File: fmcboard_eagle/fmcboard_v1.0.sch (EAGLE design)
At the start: 7 parts, among them J1 8pin, J12 4p-2.54, J2 ASP-134604-01

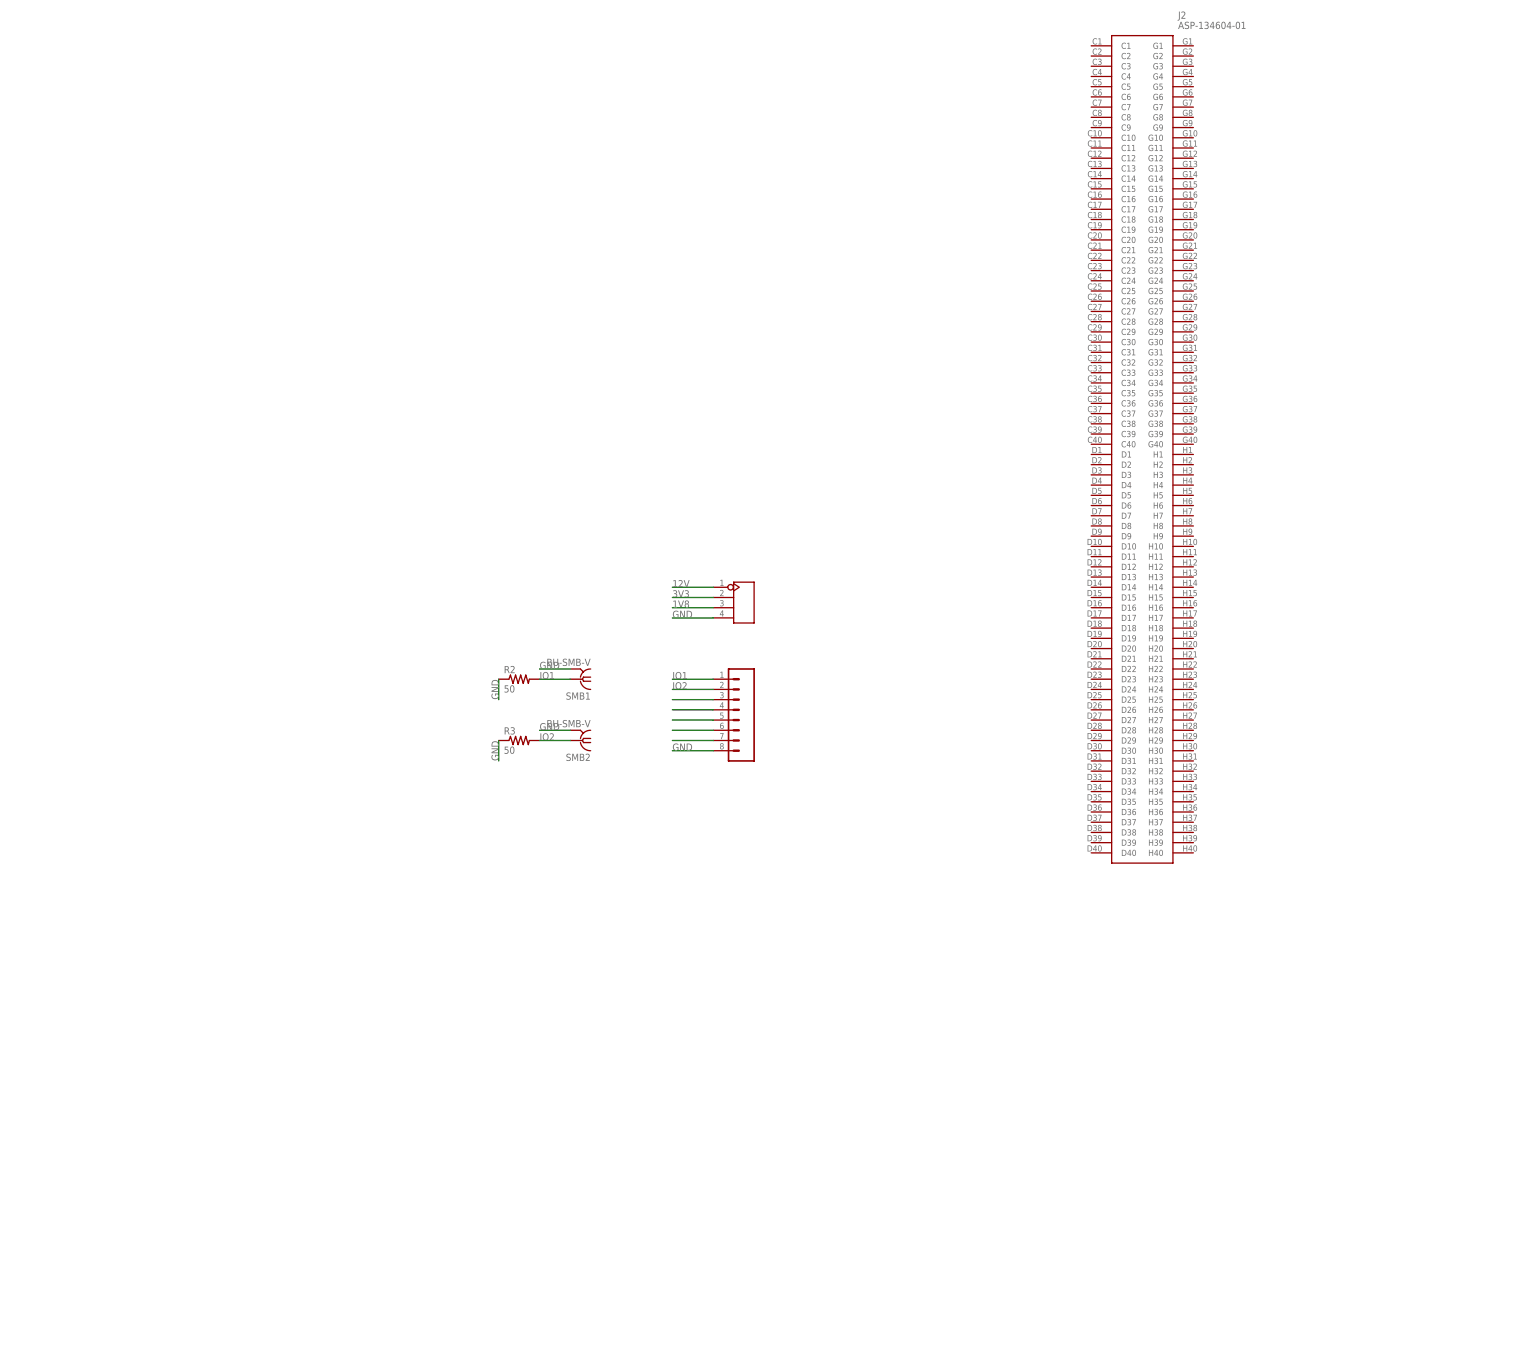
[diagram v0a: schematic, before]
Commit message: added two op amps to condition input and added GPIO breakout
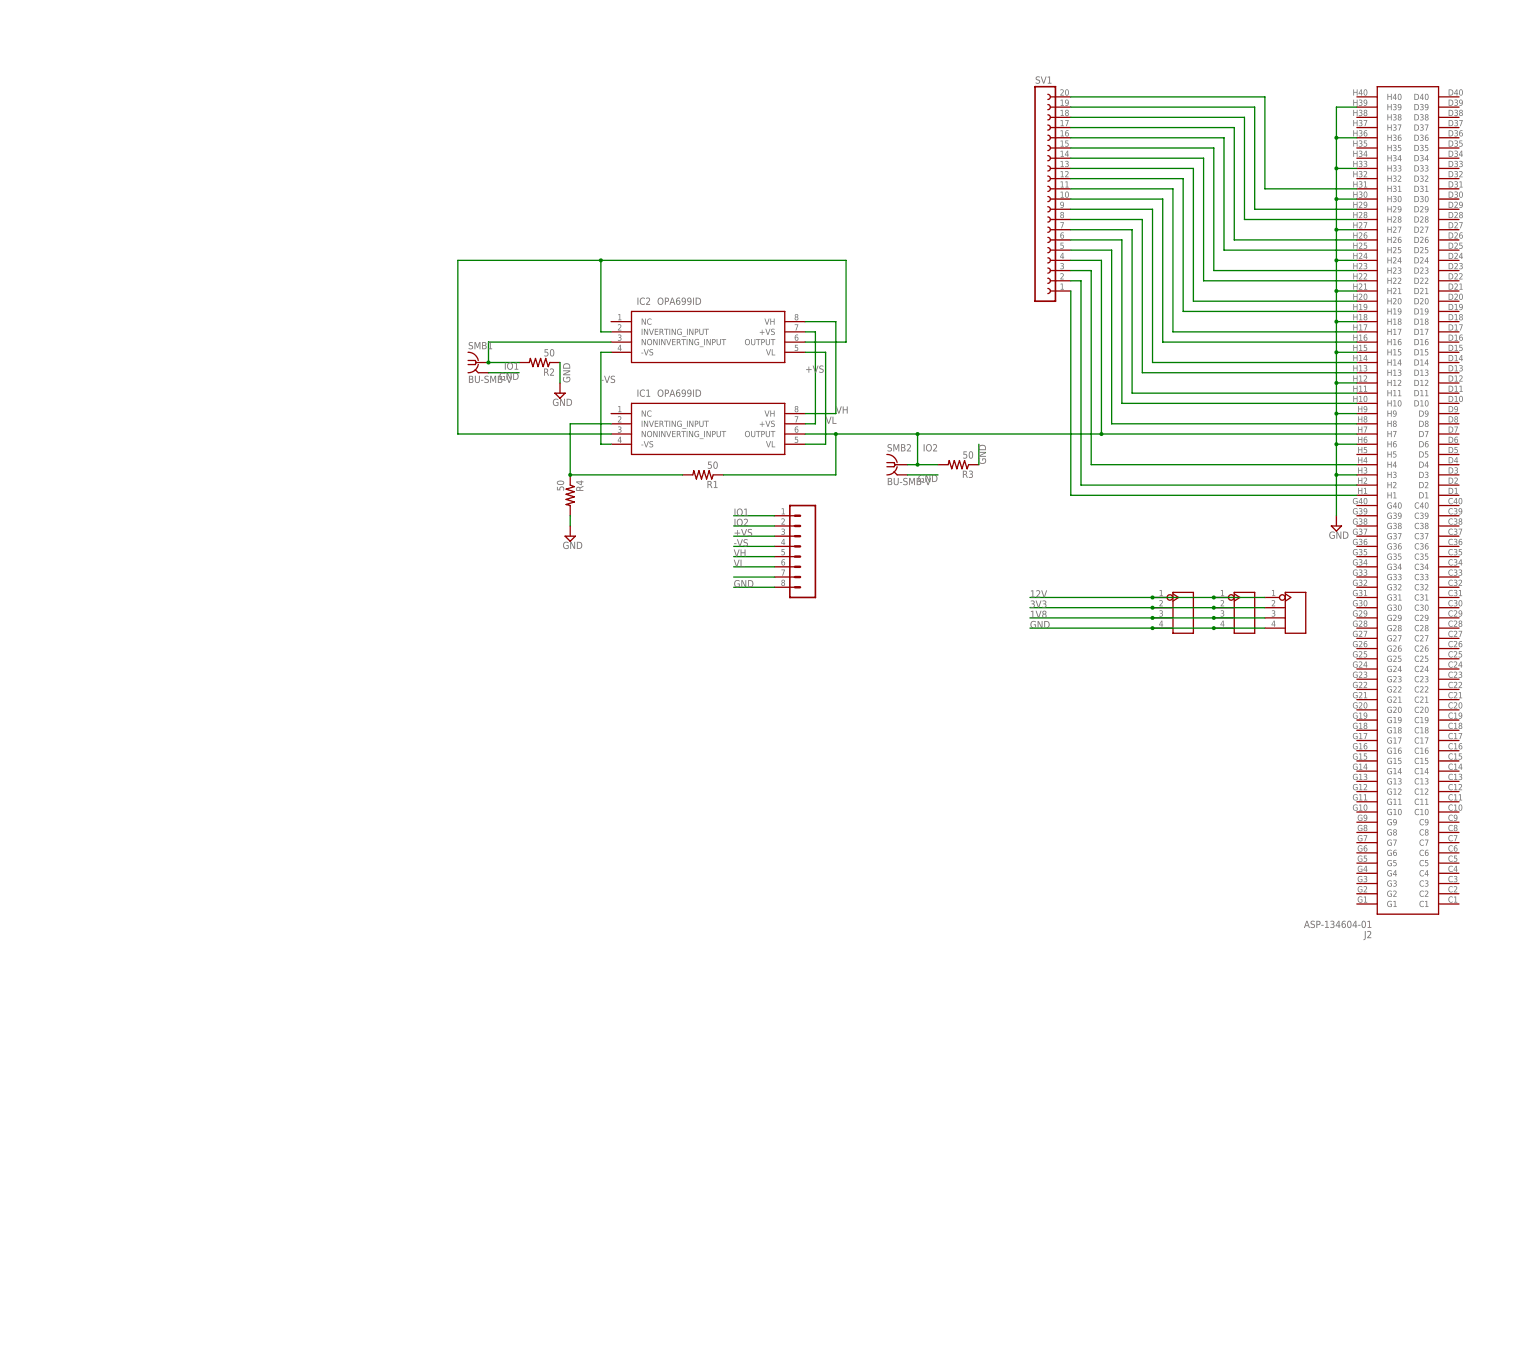
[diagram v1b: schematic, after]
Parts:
- added IC1, IC2: OPA699ID, OPA699ID:OPA699ID
- added J3, J4: 4p-2.54, Seeed-Connector:DIP-BLACK-FEMALE-HEADER-VERT(4P-2.54)
- added R1, R4: 50, SparkFun-Resistors:RESISTORAXIAL-0.3
- added SV1: (no value), con-lsta:FE20-1
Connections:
- removed net N$2: J1.3
- removed net N$4: J1.5
- removed net N$5: J1.4
- removed net N$6: J1.6
- new net +VS: IC1.+VS, IC2.+VS, J1.3
- new net -VS: IC1.-VS, IC2.-VS, J1.4
- new net N$1: IC1.NONINVERTING_INPUT, IC2.INVERTING_INPUT, IC2.OUTPUT
- new net N$10: J2.H8, SV1.5
- new net N$11: J2.H4, SV1.3
- new net N$12: J2.H10, SV1.6
- new net N$13: J2.H11, SV1.7
- new net N$14: J2.H13, SV1.8
- new net N$15: J2.H14, SV1.9
- new net N$16: J2.H16, SV1.10
- new net N$17: J2.H17, SV1.11
- new net N$18: J2.H19, SV1.12
- new net N$19: J2.H20, SV1.13
- new net N$20: J2.H22, SV1.14
- new net N$21: J2.H23, SV1.15
- new net N$22: J2.H25, SV1.16
- new net N$23: J2.H26, SV1.17
- new net N$24: J2.H28, SV1.18
- new net N$25: J2.H29, SV1.19
- new net N$26: J2.H31, SV1.20
- new net N$3: IC1.INVERTING_INPUT, R1.2, R4.1
- new net N$8: J2.H1, SV1.1
- new net N$9: J2.H2, SV1.2
- new net VH: IC1.VH, IC2.VH, J1.5
- new net VL: IC1.VL, IC2.VL, J1.6
- net 12V: now also J3.P$1, J4.P$1
- net 1V8: now also J3.P$3, J4.P$3
- net 3V3: now also J3.P$2, J4.P$2
- net GND: now also J2.H12, J2.H15, J2.H18, J2.H21, J2.H24, J2.H27, J2.H3, J2.H30, J2.H33, J2.H36, J2.H39, J2.H6, J2.H9, J3.P$4, J4.P$4, R4.2
- net IO1: now also IC2.NONINVERTING_INPUT
- net IO2: now also IC1.OUTPUT, J2.H7, R1.1, SV1.4
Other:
- moved on the sheet: J2, R2, R3, SMB1, SMB2

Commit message: board v1 work with Andre
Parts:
- added C1, C2, C4, C6: 10uF, SparkFun-Capacitors:CAPPTH1
- added C10, C11, C12, C13, C14, C3, C5, C7, C8, C9: 0.1uF, SparkFun-Passives:CAP0805
- added IC3, IC4: ICL7660CPA, maxim:ICL7660CPA
- added J5: 8pin, SparkFun-Connectors:CONN_08"
- added PCB1: ARDUINO_NANO, E14_Arduino_revC:ARDUINO_NANO
- added R5: 10k, SparkFun-Resistors:RESISTORAXIAL-0.3
- added R6: 50, SparkFun-Resistors:RESISTORAXIAL-0.3
- added R7, R8: 100k, resistor:R-TRIMM3296W
- added SMB3: BU-SMB-V, con-coax:BU-SMB-V
- added SV2: 20, con-lsta:FE20-1
- added U1: TXS0108EPWR-TSSOP20, Seeed-IC:LOGIC-TXS0108EPWR(TSSOP20)
- R1: value 50 -> 750
- R3: value 50 -> 10k
- R4: value 50 -> 150
- SV1: value (none) -> 20
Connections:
- net N$16 renamed H16
- net N$17 renamed H17
- removed net IO2: IC1.OUTPUT, J1.2, J2.H7, R1.1, R3.2, SMB2.1, SV1.4
- removed net N$10: J2.H8, SV1.5
- removed net N$11: J2.H4, SV1.3
- removed net N$12: J2.H10, SV1.6
- removed net N$13: J2.H11, SV1.7
- removed net N$14: J2.H13, SV1.8
- removed net N$15: J2.H14, SV1.9
- removed net N$18: J2.H19, SV1.12
- removed net N$19: J2.H20, SV1.13
- removed net N$20: J2.H22, SV1.14
- removed net N$21: J2.H23, SV1.15
- removed net N$22: J2.H25, SV1.16
- removed net N$23: J2.H26, SV1.17
- removed net N$24: J2.H28, SV1.18
- removed net N$25: J2.H29, SV1.19
- removed net N$26: J2.H31, SV1.20
- removed net N$7: J1.7
- removed net N$8: J2.H1, SV1.1
- removed net N$9: J2.H2, SV1.2
- new net AR_SCLIN: J5.7, PCB1.D9, U1.A7
- new net AR_SDAIN: J5.6, PCB1.D11, U1.A2
- new net H13: J2.H13, SV1.7
- new net H14: J2.H14, SV1.8
- new net H19: J2.H19, SV1.13
- new net H20: J2.H20, SV1.14
- new net H22: J2.H22, SV1.16
- new net H23: J2.H23, SV1.17
- new net H25: J2.H25, SV1.19
- new net H26: J2.H26, SV1.20
- new net H27: J2.H28, SV2.1
- new net H28: J2.H29, SV2.2
- new net H31: J2.H31, SV2.4
- new net H32: J2.H32, SV2.5
- new net H34: J2.H34, SV2.7
- new net H35: J2.H35, SV2.8
- new net H37: J2.H37, SV2.10
- new net H38: J2.H38, SV2.11
- new net IO2_H11: J2.H11, J5.2, R6.2, SMB3.1, SV1.5
- new net N$2: C4.1, IC3.CAP+
- new net N$4: C4.2, IC3.CAP-
- new net N$5: C1.1, IC4.CAP+
- new net N$6: C1.2, IC4.CAP-
- new net OFFSETIN1: C11.1, J5.4, R5.2
- new net OPBUF1: IC2.INVERTING_INPUT, IC2.OUTPUT, J5.5, R3.2
- new net OPOUT1_H10: IC1.OUTPUT, J2.H10, J5.3, R1.1, SMB2.1, SV1.4
- new net SCLIN: J2.H7, SV1.1, U1.B7
- new net SDAIN: J2.H8, SV1.2, U1.B2
- net +VS: now also C3.1, C9.1, IC3.V+, IC4.V+, PCB1.5V, R7.E, U1.VCCB
- net -VS: now also C10.1, C2.1, C6.1, IC3.VOUT, IC4.VOUT, R8.E
- net 12V: now also C12.1, J2.C37
- net 1V8: now also C14.1, C5.1, J2.H40, U1.OE, U1.VCCA
- net 3V3: now also C13.1, J2.D40
- net GND: now also C10.2, C11.2, C12.2, C13.2, C14.2, C2.2, C3.2, C5.2, C6.2, C7.2, C8.2, C9.2, IC3.GND, IC4.GND, J1.1, J1.2, J1.7, J5.8, PCB1.GND, R6.1, R7.A, R8.A, SMB3.2, SV2.17, SV2.18, SV2.19, SV2.20, U1.GND; no longer R3.1
- net IO1: now also J5.1; no longer J1.1
- net N$1: now also R3.1, R5.1; no longer IC2.INVERTING_INPUT, IC2.OUTPUT
- net VH: now also C7.1, R7.S
- net VL: now also C8.1, R8.S
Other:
- note added: "FMC breakout"
- note added: "IO"
- note added: "Level shifter"
- note added: "Negative V supply"
- note added: "Op amps"
- note added: "Power inputs"
- moved on the sheet: IC1, IC2, R1, R2, R3, R4, SMB1, SMB2

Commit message: first draft of pcb routing
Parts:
- removed PCB1: ARDUINO_NANO, E14_Arduino_revC:ARDUINO_NANO
- added ARDUINO_NANO1: (no value), ArduinoNanoV30:ARDUINO_NANO
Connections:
- net +VS: now also ARDUINO_NANO1.5V; no longer PCB1.5V
- net AR_SCLIN: now also ARDUINO_NANO1.D9; no longer PCB1.D9
- net AR_SDAIN: now also ARDUINO_NANO1.D11; no longer PCB1.D11
- net GND: now also ARDUINO_NANO1.GND@1; no longer PCB1.GND
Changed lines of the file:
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@@
 <part name="SUPPLY22" library="supply2" library_urn="urn:adsk.eagle:library:372" deviceset="GND" device=""/>
 <part name="SUPPLY23" library="supply2" library_urn="urn:adsk.eagle:library:372" deviceset="GND" device=""/>
-<part name="PCB1" library="E14_Arduino_revC" deviceset="ARDUINO_NANO" device=""/>
 <part name="SUPPLY24" library="supply2" library_urn="urn:adsk.eagle:library:372" deviceset="GND" device=""/>
+<part name="ARDUINO_NANO1" library="ArduinoNanoV30" deviceset="ARDUINO_NANO" device=""/>
 </parts>
 <sheets>
@@
 <instance part="SUPPLY22" gate="GND" x="154.94" y="20.32" smashed="yes"/>
 <instance part="SUPPLY23" gate="GND" x="170.18" y="20.32" smashed="yes"/>
-<instance part="PCB1" gate="G$1" x="45.72" y="-55.88" smashed="yes" rot="R270"/>
 <instance part="SUPPLY24" gate="GND" x="68.58" y="-68.58" smashed="yes"/>
+<instance part="ARDUINO_NANO1" gate="G$1" x="40.64" y="-60.96" smashed="yes" rot="R180">
+<attribute name="NAME" x="55.88" y="-30.48" size="1.778" layer="95" rot="R180"/>
+<attribute name="VALUE" x="55.88" y="-27.94" size="1.778" layer="96" rot="R180"/>
+</instance>
 </instances>
 <busses>
@@
 </segment>
 <segment>
-<pinref part="PCB1" gate="G$1" pin="GND"/>
 <wire x1="60.96" y1="-66.04" x2="68.58" y2="-66.04" width="0.1524" layer="91"/>
 <pinref part="SUPPLY24" gate="GND" pin="GND"/>
+<pinref part="ARDUINO_NANO1" gate="G$1" pin="GND@1"/>
 </segment>
 </net>
@@
 </segment>
 <segment>
-<pinref part="PCB1" gate="G$1" pin="5V"/>
-<wire x1="27.94" y1="-66.04" x2="20.32" y2="-66.04" width="0.1524" layer="91"/>
-<label x="20.32" y="-66.04" size="1.778" layer="95"/>
+<wire x1="20.32" y1="-66.04" x2="12.7" y2="-66.04" width="0.1524" layer="91"/>
+<label x="7.62" y="-66.04" size="1.778" layer="95"/>
+<pinref part="ARDUINO_NANO1" gate="G$1" pin="5V"/>
 </segment>
 </net>
@@
 </segment>
 <segment>
-<pinref part="PCB1" gate="G$1" pin="D11"/>
 <wire x1="60.96" y1="-40.64" x2="68.58" y2="-40.64" width="0.1524" layer="91"/>
 <label x="66.04" y="-40.64" size="1.778" layer="95"/>
+<pinref part="ARDUINO_NANO1" gate="G$1" pin="D11"/>
 </segment>
 </net>
@@
 </segment>
 <segment>
-<pinref part="PCB1" gate="G$1" pin="D9"/>
 <wire x1="60.96" y1="-45.72" x2="68.58" y2="-45.72" width="0.1524" layer="91"/>
 <label x="66.04" y="-45.72" size="1.778" layer="95"/>
+<pinref part="ARDUINO_NANO1" gate="G$1" pin="D9"/>
 </segment>
 </net>
@@
 </drawing>
 <compatibility>
+<note version="6.3" minversion="6.2.2" severity="warning">
+Since Version 6.2.2 text objects can contain more than one line,
+which will not be processed correctly with this version.
+</note>
 <note version="8.2" severity="warning">
 Since Version 8.2, EAGLE supports online libraries. The ids

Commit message: fmcboard v1 submitted
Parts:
- U1: value TXS0108EPWR-TSSOP20 -> TXS0108EPWR
- renumbered SMB1 to OPIN, SMB2 to OPOUT_H10, SMB3 to IO_H11
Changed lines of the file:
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@@
 <part name="J12" library="Seeed-Connector" library_urn="urn:adsk.eagle:library:478" deviceset="DIP-BLACK-FEMALE-HEADER-VERT(4P-2.54)" device="" package3d_urn="urn:adsk.eagle:package:33137/1" value="4p-2.54"/>
 <part name="J1" library="SparkFun-Connectors" library_urn="urn:adsk.eagle:library:513" deviceset="CONN_08" device="&quot;" package3d_urn="urn:adsk.eagle:package:38138/1" value="8pin"/>
-<part name="SMB1" library="con-coax" library_urn="urn:adsk.eagle:library:133" deviceset="BU-SMB-V" device="" package3d_urn="urn:adsk.eagle:package:6209/1"/>
-<part name="SMB2" library="con-coax" library_urn="urn:adsk.eagle:library:133" deviceset="BU-SMB-V" device="" package3d_urn="urn:adsk.eagle:package:6209/1"/>
+<part name="OPIN" library="con-coax" library_urn="urn:adsk.eagle:library:133" deviceset="BU-SMB-V" device="" package3d_urn="urn:adsk.eagle:package:6209/1"/>
+<part name="OPOUT_H10" library="con-coax" library_urn="urn:adsk.eagle:library:133" deviceset="BU-SMB-V" device="" package3d_urn="urn:adsk.eagle:package:6209/1"/>
 <part name="R2" library="SparkFun-Resistors" deviceset="RESISTOR" device="AXIAL-0.3" value="50"/>
 <part name="J2" library="ASP-134604-01" deviceset="ASP-134604-01" device=""/>
@@
 <part name="SUPPLY6" library="supply2" library_urn="urn:adsk.eagle:library:372" deviceset="GND" device=""/>
 <part name="SUPPLY7" library="supply2" library_urn="urn:adsk.eagle:library:372" deviceset="GND" device=""/>
-<part name="U1" library="Seeed-IC" library_urn="urn:adsk.eagle:library:470" deviceset="LOGIC-TXS0108EPWR(TSSOP20)" device="" package3d_urn="urn:adsk.eagle:package:32642/1" value="TXS0108EPWR-TSSOP20"/>
+<part name="U1" library="Seeed-IC" library_urn="urn:adsk.eagle:library:470" deviceset="LOGIC-TXS0108EPWR(TSSOP20)" device="" package3d_urn="urn:adsk.eagle:package:32642/1" value="TXS0108EPWR"/>
 <part name="SUPPLY8" library="supply2" library_urn="urn:adsk.eagle:library:372" deviceset="GND" device=""/>
 <part name="C3" library="SparkFun-Passives" deviceset="CAP" device="0805" value="0.1uF"/>
@@
 <part name="SUPPLY17" library="supply2" library_urn="urn:adsk.eagle:library:372" deviceset="GND" device=""/>
 <part name="SUPPLY18" library="supply2" library_urn="urn:adsk.eagle:library:372" deviceset="GND" device=""/>
-<part name="SMB3" library="con-coax" library_urn="urn:adsk.eagle:library:133" deviceset="BU-SMB-V" device="" package3d_urn="urn:adsk.eagle:package:6209/1"/>
+<part name="IO_H11" library="con-coax" library_urn="urn:adsk.eagle:library:133" deviceset="BU-SMB-V" device="" package3d_urn="urn:adsk.eagle:package:6209/1"/>
 <part name="R6" library="SparkFun-Resistors" deviceset="RESISTOR" device="AXIAL-0.3" value="50"/>
 <part name="SUPPLY19" library="supply2" library_urn="urn:adsk.eagle:library:372" deviceset="GND" device=""/>
@@
 <instance part="J12" gate="G$1" x="167.64" y="1.27" smashed="yes"/>
 <instance part="J1" gate="G$1" x="137.16" y="30.48" smashed="yes" rot="R180"/>
-<instance part="SMB1" gate="G1" x="20.32" y="162.56" smashed="yes">
+<instance part="OPIN" gate="G1" x="20.32" y="162.56" smashed="yes">
 <attribute name="NAME" x="15.24" y="165.862" size="1.778" layer="95"/>
 </instance>
-<instance part="SMB2" gate="G1" x="119.38" y="137.16" smashed="yes" rot="MR0">
+<instance part="OPOUT_H10" gate="G1" x="119.38" y="137.16" smashed="yes" rot="MR0">
 <attribute name="NAME" x="124.46" y="140.462" size="1.778" layer="95" rot="MR0"/>
 </instance>
@@
 <instance part="SUPPLY17" gate="GND" x="111.76" y="-2.54" smashed="yes"/>
 <instance part="SUPPLY18" gate="GND" x="20.32" y="124.46" smashed="yes"/>
-<instance part="SMB3" gate="G1" x="22.86" y="86.36" smashed="yes">
+<instance part="IO_H11" gate="G1" x="22.86" y="86.36" smashed="yes">
 <attribute name="NAME" x="17.78" y="89.662" size="1.778" layer="95"/>
 </instance>
@@
 <net name="GND" class="1">
 <segment>
-<pinref part="SMB2" gate="G1" pin="2"/>
+<pinref part="OPOUT_H10" gate="G1" pin="2"/>
 <wire x1="116.84" y1="134.62" x2="116.84" y2="132.08" width="0.1524" layer="91"/>
 <pinref part="SUPPLY4" gate="GND" pin="GND"/>
@@
 </segment>
 <segment>
-<pinref part="SMB1" gate="G1" pin="2"/>
+<pinref part="OPIN" gate="G1" pin="2"/>
 <pinref part="SUPPLY5" gate="GND" pin="GND"/>
 <wire x1="22.86" y1="157.48" x2="22.86" y2="160.02" width="0.1524" layer="91"/>
@@
 </segment>
 <segment>
-<pinref part="SMB3" gate="G1" pin="2"/>
+<pinref part="IO_H11" gate="G1" pin="2"/>
 <pinref part="SUPPLY19" gate="GND" pin="GND"/>
 <wire x1="25.4" y1="81.28" x2="25.4" y2="83.82" width="0.1524" layer="91"/>
@@
 <net name="IO1" class="0">
 <segment>
-<pinref part="SMB1" gate="G1" pin="1"/>
+<pinref part="OPIN" gate="G1" pin="1"/>
 <label x="12.7" y="165.1" size="1.778" layer="95" rot="R180"/>
 <wire x1="22.86" y1="162.56" x2="22.86" y2="167.64" width="0.1524" layer="91"/>
@@
 </segment>
 </net>
-<net name="1V8" class="0">
+<net name="1V8" class="1">
 <segment>
 <pinref part="J12" gate="G$1" pin="P$3"/>
@@
 </segment>
 </net>
-<net name="3V3" class="0">
+<net name="3V3" class="1">
 <segment>
 <pinref part="J12" gate="G$1" pin="P$2"/>
@@
 </segment>
 </net>
-<net name="12V" class="0">
+<net name="12V" class="1">
 <segment>
 <pinref part="J12" gate="G$1" pin="P$1"/>
@@
 </segment>
 </net>
-<net name="+VS" class="0">
+<net name="+VS" class="1">
 <segment>
 <pinref part="IC1" gate="G$1" pin="+VS"/>
@@
 </segment>
 </net>
-<net name="-VS" class="0">
+<net name="-VS" class="1">
 <segment>
 <pinref part="IC2" gate="G$1" pin="-VS"/>
@@
 <net name="OPOUT1_H10" class="0">
 <segment>
-<pinref part="SMB2" gate="G1" pin="1"/>
+<pinref part="OPOUT_H10" gate="G1" pin="1"/>
 <wire x1="116.84" y1="144.78" x2="116.84" y2="137.16" width="0.1524" layer="91"/>
 <pinref part="IC1" gate="G$1" pin="OUTPUT"/>
@@
 <net name="IO2_H11" class="0">
 <segment>
-<pinref part="SMB3" gate="G1" pin="1"/>
+<pinref part="IO_H11" gate="G1" pin="1"/>
 <label x="15.24" y="88.9" size="1.778" layer="95" rot="R180"/>
 <pinref part="R6" gate="G$1" pin="2"/>
